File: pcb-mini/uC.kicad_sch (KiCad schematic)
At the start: 37 parts, among them J14 SM03B-SRSS-TB, SW7 SW_Push, SW8 SW_Push, U2 RP2350_80QFN, U6 W25Q128JVS, Y2 ABM8-272-T3

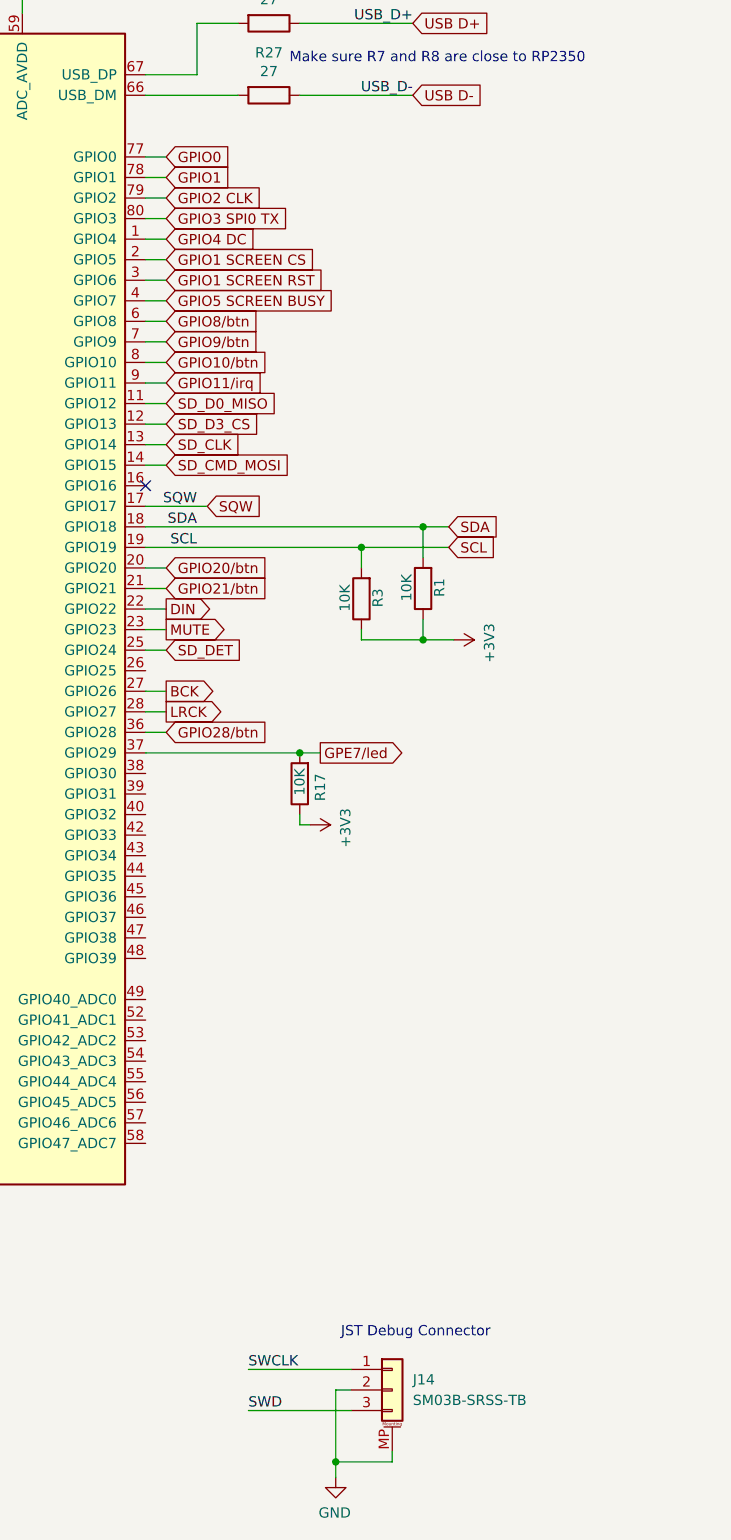
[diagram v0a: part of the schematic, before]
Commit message: [pcb-mini] add ESP32, RM2, route most things
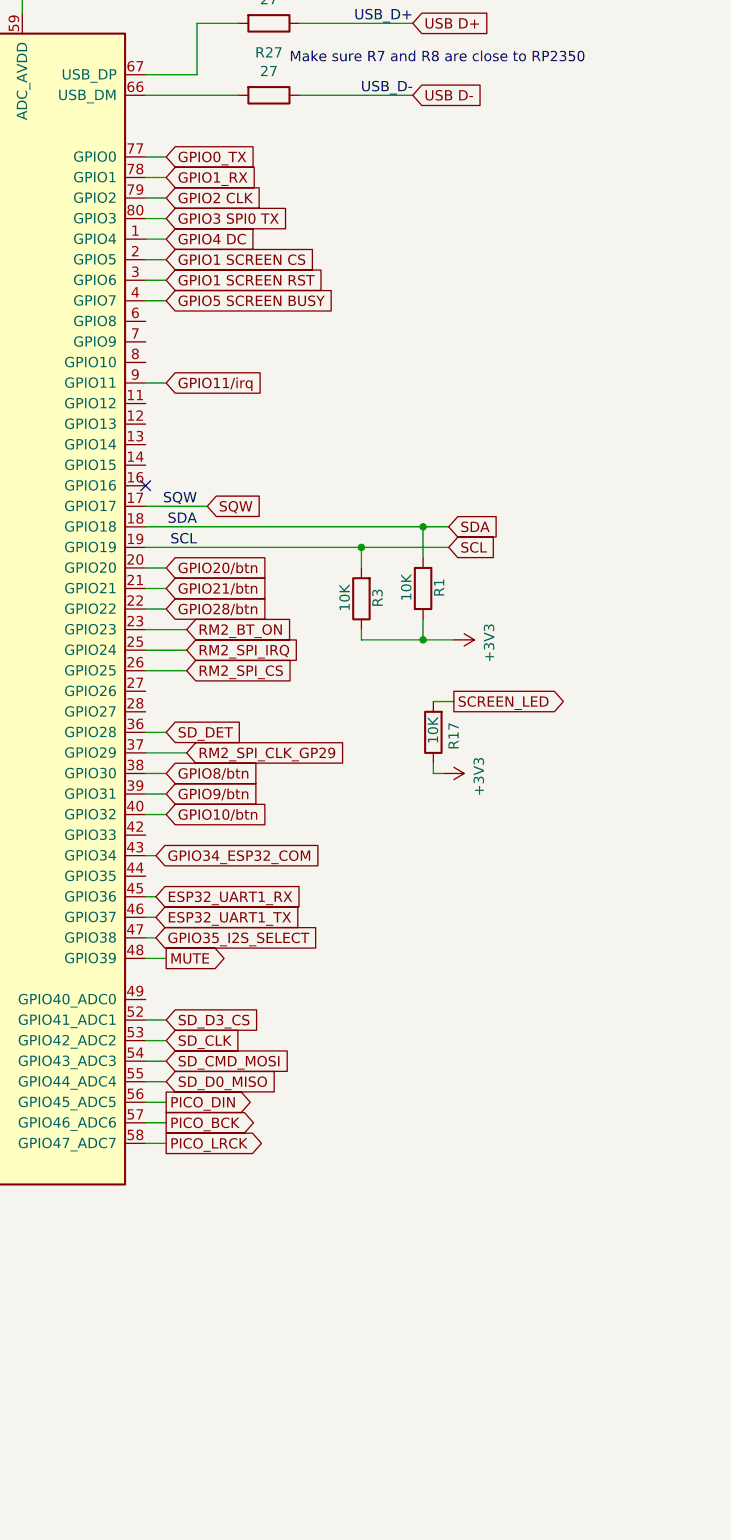
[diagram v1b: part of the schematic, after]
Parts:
- removed J14: SM03B-SRSS-TB, Connector_JST:JST_SH_SM03B-SRSS-TB_1x03-1MP_P1.00mm_Horizontal, symbol Connector_Generic_MountingPin:Conn_01x03_MountingPin
- U6: footprint Package_SO:SOIC-8_5.23x5.23mm_P1.27mm -> Package_SO:SOIC-8_5.3x5.3mm_P1.27mm
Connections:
- net DIN is gone; now on net GPIO28/btn: U2.22 (GPIO22)
- net GPIO0: no longer U2.77 (GPIO0)
- net GPIO10/btn: now also U2.40 (GPIO32); no longer U2.8 (GPIO10)
- net GPIO28/btn: no longer U2.36 (GPIO28)
- net GPIO8/btn: now also U2.38 (GPIO30); no longer U2.6 (GPIO8)
- net GPIO9/btn: now also U2.39 (GPIO31); no longer U2.7 (GPIO9)
- net MUTE: now also U2.48 (GPIO39); no longer U2.23 (GPIO23)
- net SD_CLK: now also U2.53 (GPIO42_ADC2); no longer U2.13 (GPIO14)
- net SD_CMD_MOSI: now also U2.54 (GPIO43_ADC3); no longer U2.14 (GPIO15)
- net SD_D0_MISO: now also U2.55 (GPIO44_ADC4); no longer U2.11 (GPIO12)
- net SD_D3_CS: now also U2.52 (GPIO41_ADC1); no longer U2.12 (GPIO13)
- net SD_DET: now also U2.36 (GPIO28); no longer U2.25 (GPIO24)
- net RM2_SPI_CS: now reaches U2.26 (GPIO25)
- net GPIO34_ESP32_COM: now reaches U2.43 (GPIO34)
- net ESP32_UART1_RX: now reaches U2.45 (GPIO36)
- net ESP32_UART1_TX: now reaches U2.46 (GPIO37)
- net GPIO35_I2S_SELECT: now reaches U2.47 (GPIO38)
- net PICO_DIN: now reaches U2.56 (GPIO45_ADC5)
- net PICO_BCK: now reaches U2.57 (GPIO46_ADC6)
- net PICO_LRCK: now reaches U2.58 (GPIO47_ADC7)
- net BCK: no longer names the net of U2.27 (GPIO26)
- net GPE7/led renamed RM2_SPI_CLK_GP29
- net RM2_SPI_CLK_GP29: no longer R17.2
- net GPIO1 renamed GPIO1_RX
- net LRCK: no longer names the net of U2.28 (GPIO27)
- new net GPIO0_TX: U2.77 (GPIO0)
- new net RM2_BT_ON: U2.23 (GPIO23)
- new net RM2_SPI_IRQ: U2.25 (GPIO24)
- new net SCREEN_LED: R17.2
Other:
- note removed: "JST Debug Connector"
- moved on the sheet: R17

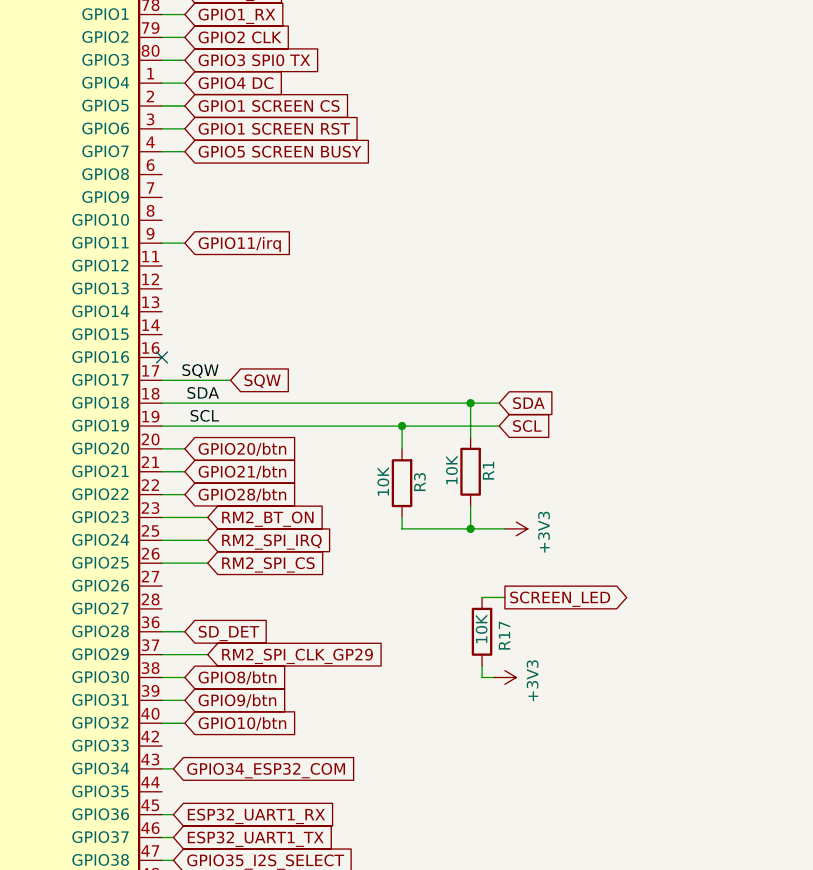
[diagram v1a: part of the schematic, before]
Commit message: [pcb-mini] fix warnings/errors
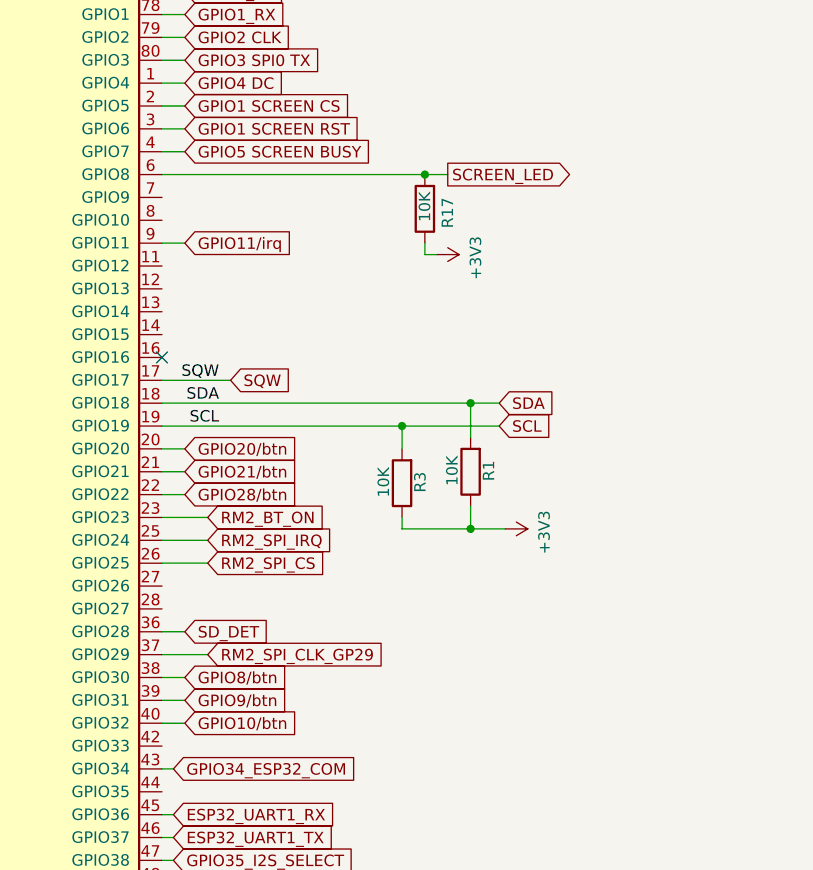
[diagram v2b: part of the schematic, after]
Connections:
- net SCREEN_LED: now also U2.6 (GPIO8)
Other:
- moved on the sheet: R17
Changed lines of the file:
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@@
 	)
 	(junction
+		(at 271.78 128.27)
+		(diameter 0)
+		(color 0 0 0 0)
+	)
+	(junction
 		(at 316.23 57.15)
 		(diameter 0)
@@
 	(wire
 		(pts
+			(xy 242.57 128.27) (xy 271.78 128.27)
+		)
+		(stroke
+			(width 0)
+			(type default)
+		)
+	)
+	(wire
+		(pts
 			(xy 243.84 201.93) (xy 242.57 201.93)
 		)
@@
 	(wire
 		(pts
-			(xy 279.4 184.15) (xy 278.13 184.15)
+			(xy 273.05 137.16) (xy 271.78 137.16)
 		)
 		(stroke
@@
 	(wire
 		(pts
-			(xy 278.13 175.26) (xy 280.67 175.26)
+			(xy 271.78 128.27) (xy 274.32 128.27)
 		)
 		(stroke
@@
 	(wire
 		(pts
-			(xy 278.13 184.15) (xy 278.13 182.88)
+			(xy 271.78 137.16) (xy 271.78 135.89)
 		)
 		(stroke
@@
 	(global_label "SCREEN_LED"
 		(shape output)
-		(at 280.67 175.26 0)
+		(at 274.32 128.27 0)
 		(fields_autoplaced yes)
 		(effects
@@
 		)
 		(property "Intersheetrefs" "${INTERSHEET_REFS}"
-			(at 295.4479 175.26 0)
+			(at 289.0979 128.27 0)
 			(effects
 				(font
@@
 	(symbol
 		(lib_id "power:+3V3")
-		(at 279.4 184.15 270)
+		(at 273.05 137.16 270)
 		(unit 1)
 		(exclude_from_sim no)
@@
 		(dnp no)
 		(property "Reference" "#PWR06"
-			(at 275.59 184.15 0)
+			(at 269.24 137.16 0)
 			(effects
 				(font
@@
 		)
 		(property "Value" "+3V3"
-			(at 283.7942 184.531 0)
+			(at 277.4442 137.541 0)
 			(effects
 				(font
@@
 		)
 		(property "Footprint" ""
-			(at 279.4 184.15 0)
+			(at 273.05 137.16 0)
 			(effects
 				(font
@@
 		)
 		(property "Datasheet" ""
-			(at 279.4 184.15 0)
+			(at 273.05 137.16 0)
 			(effects
 				(font
@@
 		)
 		(property "Description" ""
-			(at 279.4 184.15 0)
+			(at 273.05 137.16 0)
 			(effects
 				(font
@@
 	(symbol
 		(lib_id "Device:R")
-		(at 278.13 179.07 180)
+		(at 271.78 132.08 180)
 		(unit 1)
 		(exclude_from_sim no)
@@
 		(dnp no)
 		(property "Reference" "R17"
-			(at 280.67 177.8 90)
+			(at 274.32 130.81 90)
 			(effects
 				(font
@@
 		)
 		(property "Value" "10K"
-			(at 278.13 177.165 90)
+			(at 271.78 130.175 90)
 			(effects
 				(font
@@
 		)
 		(property "Footprint" "Resistor_SMD:R_0603_1608Metric"
-			(at 279.908 179.07 90)
+			(at 273.558 132.08 90)
 			(effects
 				(font
@@
 		)
 		(property "Datasheet" "~"
-			(at 278.13 179.07 0)
+			(at 271.78 132.08 0)
 			(effects
 				(font
@@
 		)
 		(property "Description" ""
-			(at 278.13 179.07 0)
+			(at 271.78 132.08 0)
 			(effects
 				(font
@@
 		)
 		(property "LCSC" "C25744"
-			(at 278.13 179.07 0)
+			(at 271.78 132.08 0)
 			(effects
 				(font

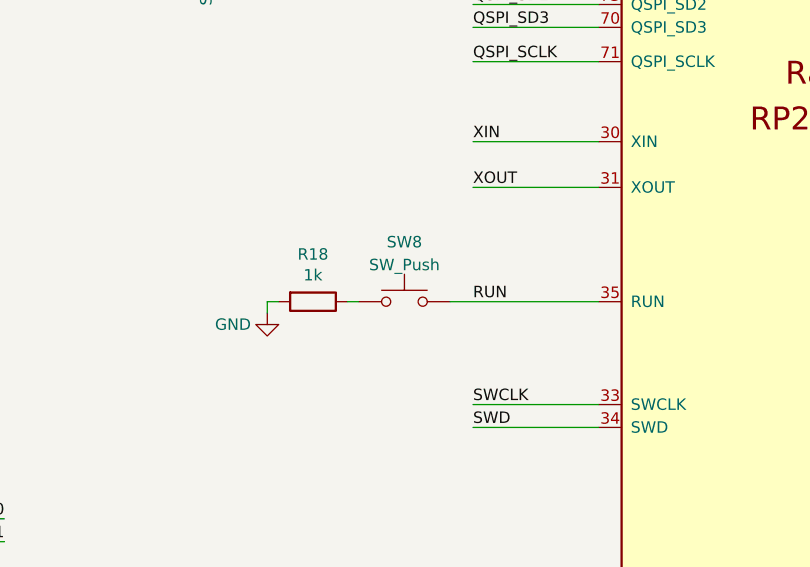
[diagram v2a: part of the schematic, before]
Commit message: [mini] add pin for screen holder in pcb + 3d
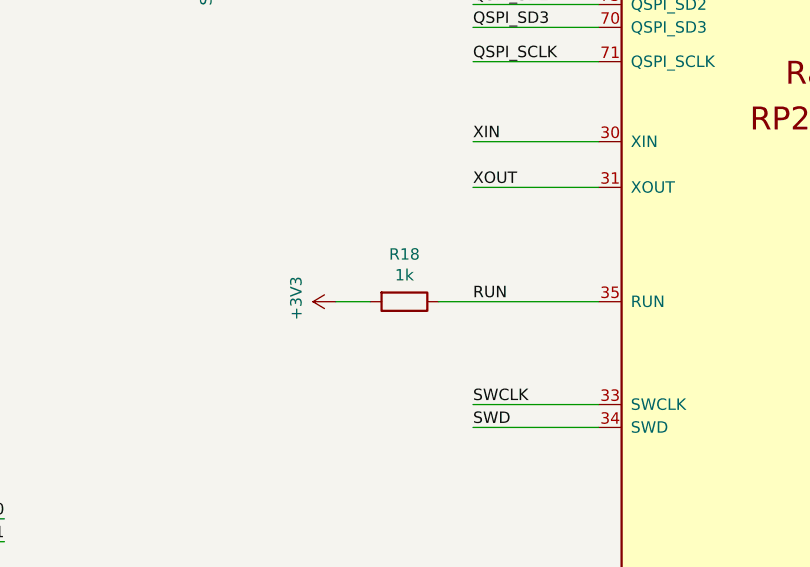
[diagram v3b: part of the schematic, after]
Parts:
- removed SW8: SW_Push, Button_Switch_SMD:SW_Push_1P1T_NO_Vertical_Wuerth_434133025816, symbol Switch:SW_Push
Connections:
- net +3V3: now also R18.2
- net GND: no longer R18.2
- net RUN: now also R18.1
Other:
- moved on the sheet: R18
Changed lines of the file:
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@@
 	(wire
 		(pts
-			(xy 137.16 161.29) (xy 137.16 162.56)
-		)
-		(stroke
-			(width 0)
-			(type default)
-		)
-	)
-	(wire
-		(pts
 			(xy 245.11 123.19) (xy 242.57 123.19)
 		)
@@
 	(wire
 		(pts
-			(xy 157.48 161.29) (xy 173.99 161.29)
-		)
-		(stroke
-			(width 0)
-			(type default)
-		)
-	)
-	(wire
-		(pts
 			(xy 280.035 153.67) (xy 276.86 153.67)
 		)
@@
 	(wire
 		(pts
+			(xy 144.78 161.29) (xy 148.59 161.29)
+		)
+		(stroke
+			(width 0)
+			(type default)
+		)
+	)
+	(wire
+		(pts
 			(xy 160.02 143.51) (xy 173.99 143.51)
 		)
@@
 	(wire
 		(pts
-			(xy 146.05 161.29) (xy 147.32 161.29)
+			(xy 156.21 161.29) (xy 173.99 161.29)
 		)
 		(stroke
@@
 	(wire
 		(pts
-			(xy 137.16 161.29) (xy 138.43 161.29)
-		)
-		(stroke
-			(width 0)
-			(type default)
-		)
-	)
-	(wire
-		(pts
 			(xy 243.84 199.39) (xy 242.57 199.39)
 		)
@@
 	)
 	(symbol
-		(lib_id "Switch:SW_Push")
-		(at 152.4 161.29 0)
-		(unit 1)
-		(exclude_from_sim no)
-		(in_bom yes)
-		(on_board yes)
-		(dnp no)
-		(fields_autoplaced yes)
-		(property "Reference" "SW8"
-			(at 152.4 154.6692 0)
-			(effects
-				(font
-					(size 1.27 1.27)
-				)
-			)
-		)
-		(property "Value" "SW_Push"
-			(at 152.4 157.2061 0)
-			(effects
-				(font
-					(size 1.27 1.27)
-				)
-			)
-		)
-		(property "Footprint" "Button_Switch_SMD:SW_Push_1P1T_NO_Vertical_Wuerth_434133025816"
-			(at 152.4 156.21 0)
-			(effects
-				(font
-					(size 1.27 1.27)
-				)
-				(hide yes)
-			)
-		)
-		(property "Datasheet" "~"
-			(at 152.4 156.21 0)
-			(effects
-				(font
-					(size 1.27 1.27)
-				)
-				(hide yes)
-			)
-		)
-		(property "Description" ""
-			(at 152.4 161.29 0)
-			(effects
-				(font
-					(size 1.27 1.27)
-				)
-			)
-		)
-		(pin "1"
-		)
-		(pin "2"
-		)
-		(instances
-			(project "picoclock"
-				(path "/3b9dec0e-e0b7-4565-afc9-c4692f41aea9/c43ebd9a-50e4-4584-b727-17a1b881c0c3"
-					(reference "SW8")
-					(unit 1)
-				)
-			)
-		)
-	)
-	(symbol
 		(lib_id "power:GND")
 		(at 88.9 177.8 0)
@@
 	)
 	(symbol
-		(lib_id "power:GND")
-		(at 137.16 162.56 0)
+		(lib_id "power:+3V3")
+		(at 144.78 161.29 90)
 		(unit 1)
 		(exclude_from_sim no)
@@
 		(on_board yes)
 		(dnp no)
-		(property "Reference" "#PWR071"
-			(at 137.16 168.91 0)
+		(property "Reference" "#PWR070"
+			(at 148.59 161.29 0)
 			(effects
 				(font
@@
 			)
 		)
-		(property "Value" "GND"
-			(at 133.35 163.83 0)
+		(property "Value" "+3V3"
+			(at 140.3858 160.909 0)
 			(effects
 				(font
@@
 		)
 		(property "Footprint" ""
-			(at 137.16 162.56 0)
+			(at 144.78 161.29 0)
 			(effects
 				(font
@@
 		)
 		(property "Datasheet" ""
-			(at 137.16 162.56 0)
+			(at 144.78 161.29 0)
 			(effects
 				(font
@@
 		)
 		(property "Description" ""
-			(at 137.16 162.56 0)
+			(at 144.78 161.29 0)
 			(effects
 				(font
@@
 			(project "picoclock"
 				(path "/3b9dec0e-e0b7-4565-afc9-c4692f41aea9/c43ebd9a-50e4-4584-b727-17a1b881c0c3"
-					(reference "#PWR071")
+					(reference "#PWR070")
 					(unit 1)
 				)
@@
 	(symbol
 		(lib_id "Device:R")
-		(at 142.24 161.29 270)
+		(at 152.4 161.29 270)
 		(unit 1)
 		(exclude_from_sim no)
@@
 		(dnp no)
 		(property "Reference" "R18"
-			(at 142.24 156.0322 90)
+			(at 152.4 156.0322 90)
 			(effects
 				(font
@@
 		)
 		(property "Value" "1k"
-			(at 142.24 158.3436 90)
+			(at 152.4 158.3436 90)
 			(effects
 				(font
@@
 		)
 		(property "Footprint" "Resistor_SMD:R_0402_1005Metric"
-			(at 142.24 159.512 90)
+			(at 152.4 159.512 90)
 			(effects
 				(font
@@
 		)
 		(property "Datasheet" "~"
-			(at 142.24 161.29 0)
+			(at 152.4 161.29 0)
 			(effects
 				(font
@@
 		)
 		(property "Description" ""
-			(at 142.24 161.29 0)
+			(at 152.4 161.29 0)
 			(effects
 				(font

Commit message: [pcb] mini: many silkscreen fixes
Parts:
- removed R18: 1k, Resistor_SMD:R_0402_1005Metric, symbol Device:R
- removed R20: DNF, Resistor_SMD:R_0402_1005Metric, symbol Device:R
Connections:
- net GPIO11/irq: no longer names the net of U2.9 (GPIO11)

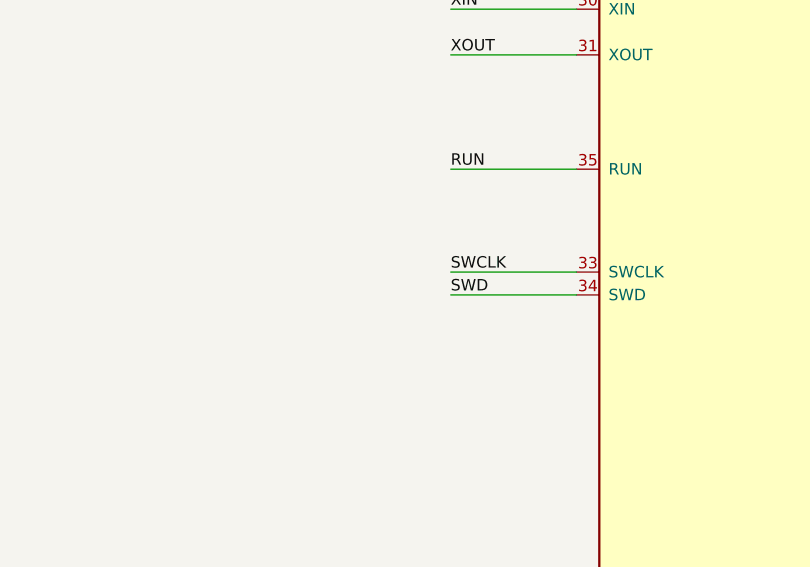
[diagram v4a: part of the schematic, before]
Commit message: [pcb] mini: add debug port, improve/fix traces
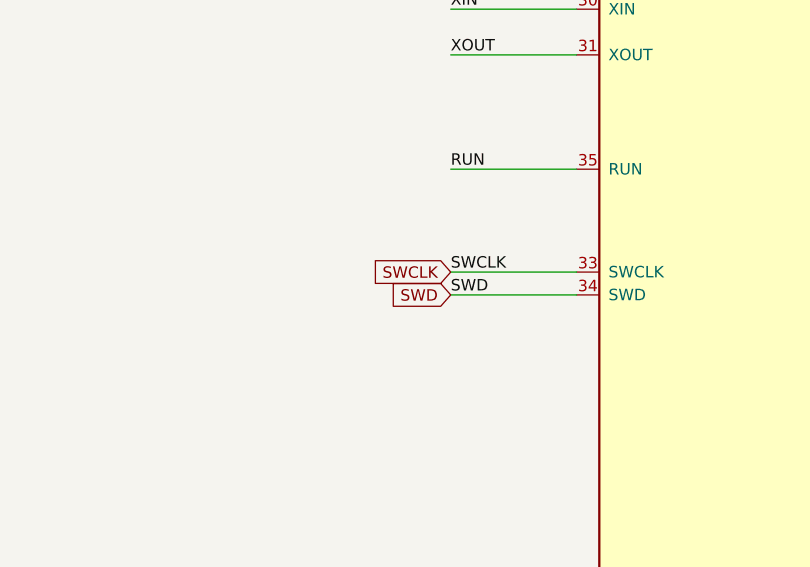
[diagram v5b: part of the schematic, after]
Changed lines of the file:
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@@
+		)
+	)
+	(global_label "SWCLK"
+		(shape input)
+		(at 160.02 172.72 180)
+		(fields_autoplaced yes)
+		(effects
+			(font
+				(size 1.27 1.27)
+			)
+			(justify right)
+		)
+		(property "Intersheetrefs" "${INTERSHEET_REFS}"
+			(at 150.8058 172.72 0)
+			(effects
+				(font
+					(size 1.27 1.27)
+				)
+				(justify right)
+				(hide yes)
+			)
 		)
 	)
@@
 				(hide yes)
 			)
+		)
+	)
+	(global_label "SWD"
+		(shape input)
+		(at 160.02 175.26 180)
+		(fields_autoplaced yes)
+		(effects
+			(font
+				(size 1.27 1.27)
+			)
+			(justify right)
+		)
+		(property "Intersheetrefs" "${INTERSHEET_REFS}"
+			(at 153.1039 175.26 0)
+			(effects
+				(font
+					(size 1.27 1.27)
+				)
+				(justify right)
+				(hide yes)
+			)
